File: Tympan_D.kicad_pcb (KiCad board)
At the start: 4 copper layers, 38 x 74 mm, 116 parts, among them IC1 MK66FX1M0VMD18, IC2 MKL02Z32VFG4, IC3 BC127, J1 SJ-3523-SMT-TR, J2 SJ-3524-SMT-TR-PI, J3 alt Power Pads, P1 USB_OTG, P10 CONN_01X01, P2 CONN_01X06, P3 CONN_01X06, P4 CONN_01X06, P5 CONN_01X06, P6 CONN_01X03, P7 CONN_01X01, P8 CONN_01X01, P9 CONN_01X01, SW1 CL-SB-22A, SW2 TACT_SWITCH, U1 AP2210K-3.3TRG1, U2 TLV320AIC3206IRSBT, U3 74LVC1G66, U4 LP5907MFX-1.8, U5 MCP73831, Y1 32.768kHz, Y2 16MHz

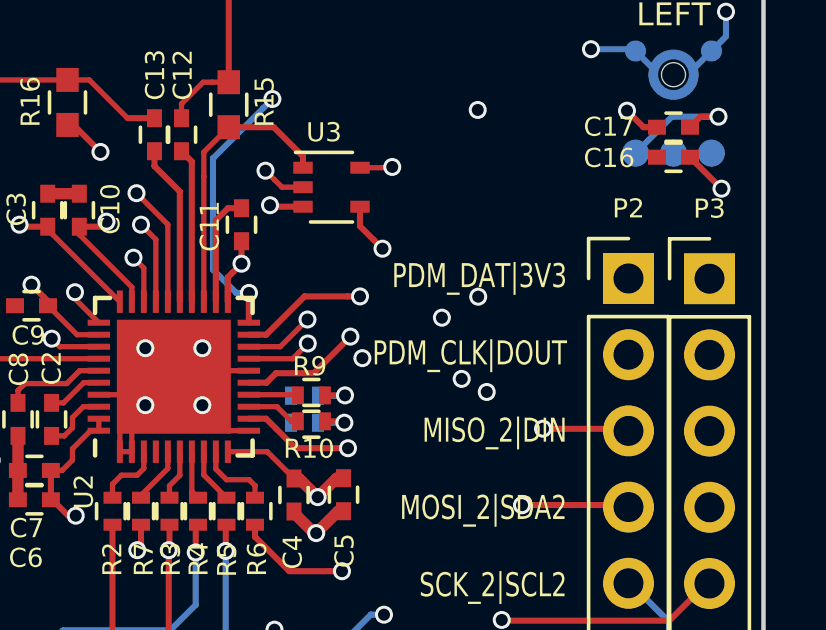
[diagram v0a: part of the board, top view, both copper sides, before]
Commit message: Changed the PDM pins
Also added Melody User Guides for reference
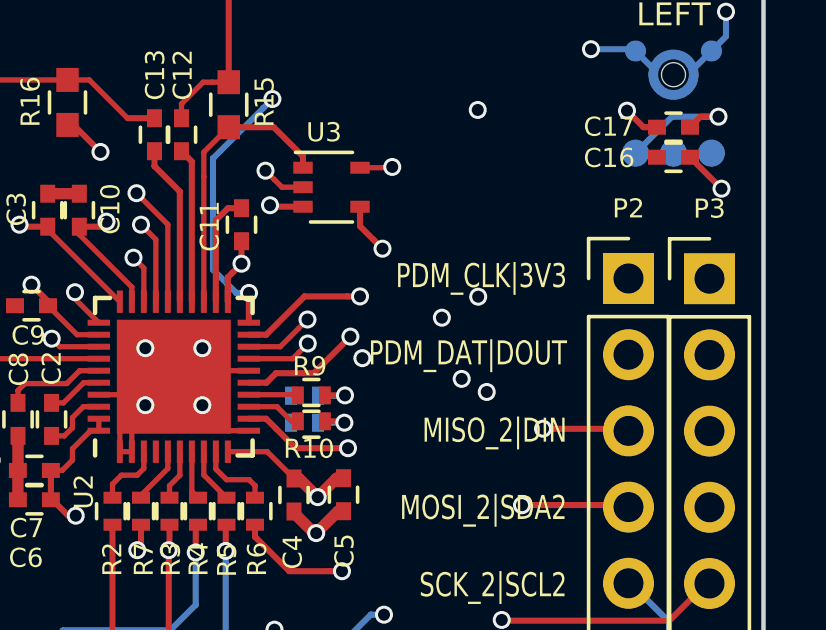
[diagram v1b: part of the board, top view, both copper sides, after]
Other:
- board text added: "PDM_CLK|3V3 PDM_DAT|DOUT MISO_2|DIN MOSI_2|SDA2 SCK_2|SCL2 SS_2|GND"
- board text removed: "PDM_DAT|3V3 PDM_CLK|DOUT MISO_2|DIN MOSI_2|SDA2 SCK_2|SCL2 SS_2|GND"
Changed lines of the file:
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@@
     (effects (font (size 0.7 0.7) (thickness 0.175)) (justify right mirror))
   )
-  (gr_text "PDM_DAT|3V3\n\nPDM_CLK|DOUT\n\nMISO_2|DIN\n\nMOSI_2|SDA2\n\nSCK_2|SCL2\n\nSS_2|GND\n" (at 146.3 78.13) (layer F.SilkS)
+  (gr_text "PDM_CLK|3V3\n\nPDM_DAT|DOUT\n\nMISO_2|DIN\n\nMOSI_2|SDA2\n\nSCK_2|SCL2\n\nSS_2|GND\n" (at 146.3 78.13) (layer F.SilkS)
     (effects (font (size 0.8 0.6) (thickness 0.15)) (justify right))
   )
